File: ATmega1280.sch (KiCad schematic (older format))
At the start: 24 parts, among them CON1 AVR-ISP-10, CON2 AVR-JTAG-10, IC1 ATMEGA1280-A, P1 CONN_02X20, P3 CONN_01X03, P4 CONN_01X03, SW1 SW_PUSH, U1 74HCT541_PWR, U6 WS2812, U7 WS2812, U8 WS2812, X1 CRYSTAL

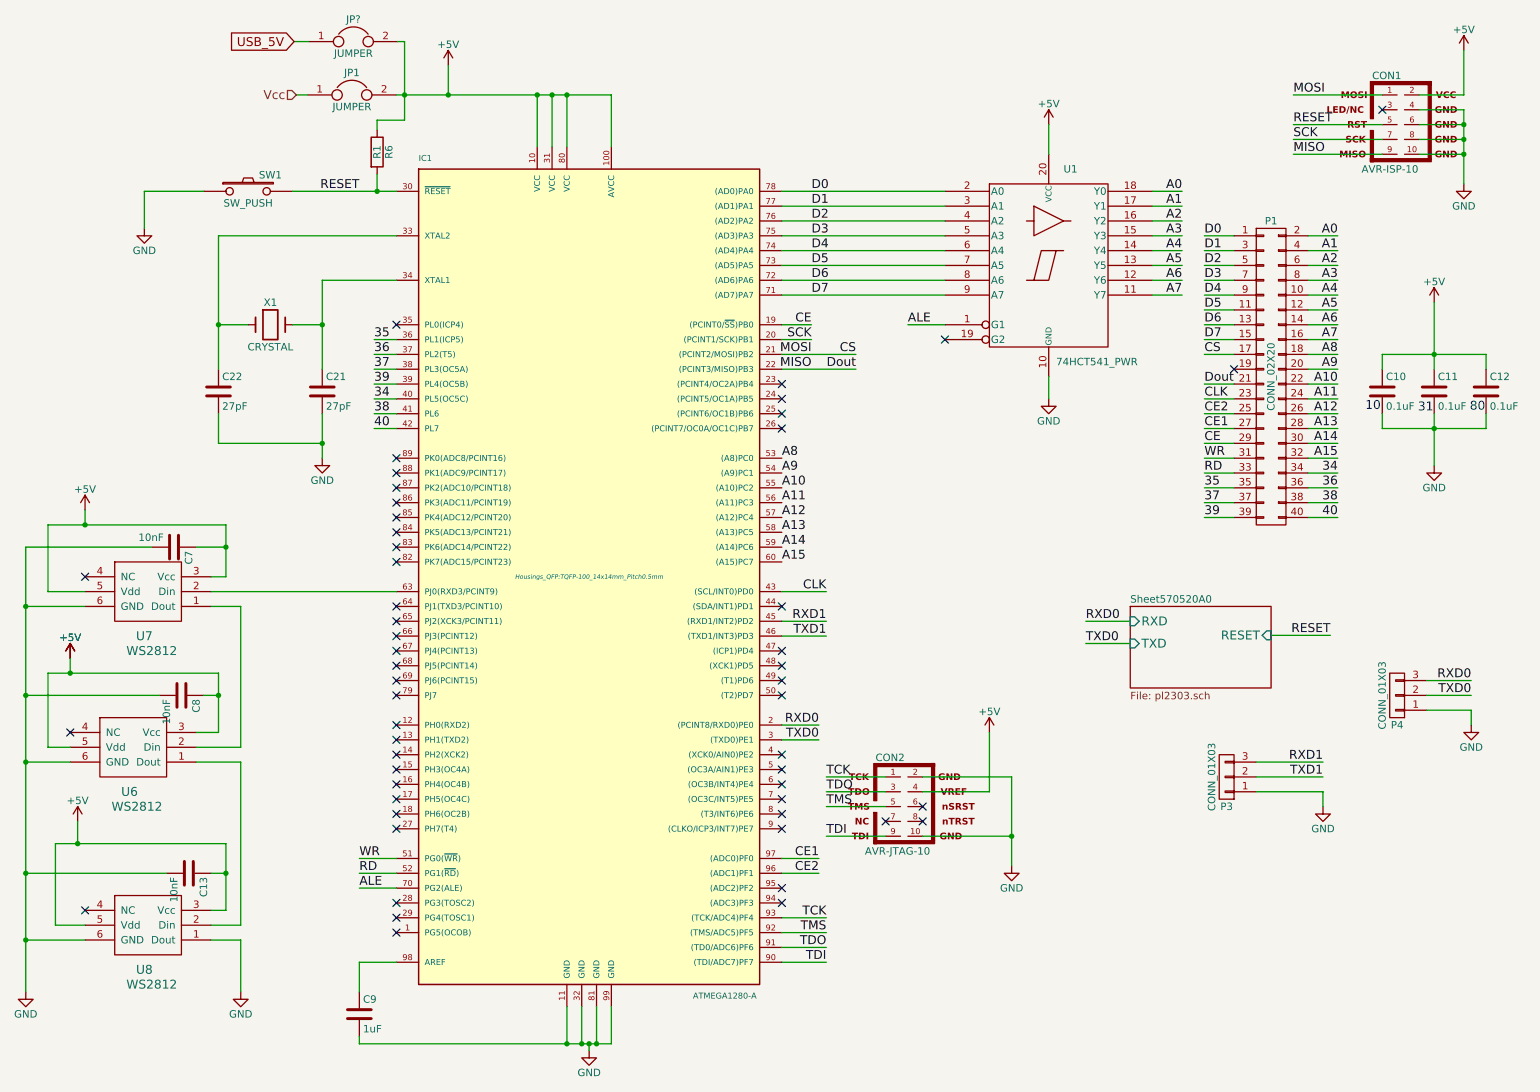
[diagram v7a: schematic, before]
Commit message: Добавлен AMS1117 и изменения в питании
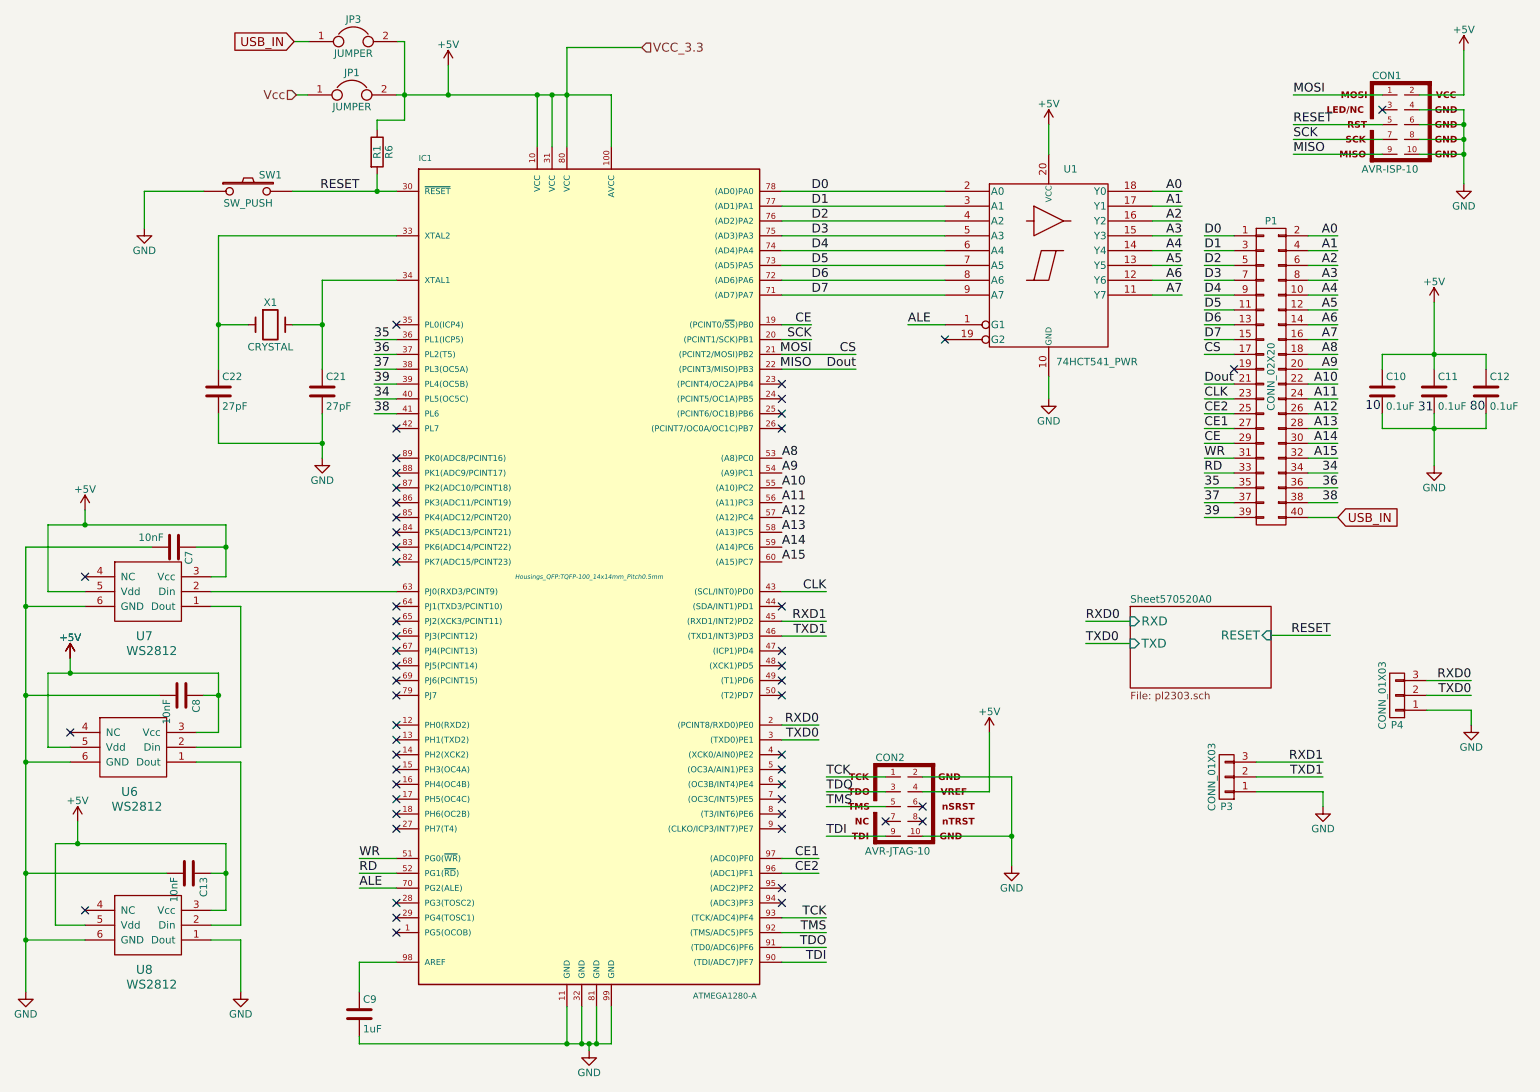
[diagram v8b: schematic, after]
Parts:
- JP3: renamed from JP?; footprint (none) -> Connect:PINHEAD1-2
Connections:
- net 40: no longer names the net of IC1.42 (PL7)
- net 40: no longer P1.40 (P40)
- net USB_5V renamed USB_IN
- net USB_IN: now also P1.40 (P40)
- no-connect marks 53 -> 54
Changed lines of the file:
@@
 $Descr A4 11693 8268
 encoding utf-8
-Sheet 2 4
+Sheet 3 4
 Title ""
 Date "20 apr 2016"
@@
 $EndComp
 $Comp
-L ATMEGA1280-A IC1
-U 1 1 56DEFC46
-P 4450 4350
-F 0 "IC1" H 3300 7150 40  0000 L BNN
-F 1 "ATMEGA1280-A" H 5150 1500 40  0000 L BNN
-F 2 "Housings_QFP:TQFP-100_14x14mm_Pitch0.5mm" H 4450 4350 30  0000 C CIN
-F 3 "" H 4450 4350 60  0000 C CNN
-	1    4450 4350
-	1    0    0    -1
-$EndComp
-$Comp
-L +5V #PWR02
+L +5V #PWR07
 U 1 1 56E703CC
 P 3500 900
-F 0 "#PWR02" H 3500 750 50  0001 C CNN
+F 0 "#PWR07" H 3500 750 50  0001 C CNN
 F 1 "+5V" H 3500 1040 50  0000 C CNN
 F 2 "" H 3500 900 50  0000 C CNN
@@
 $EndComp
 $Comp
-L GND #PWR03
+L GND #PWR08
 U 1 1 56E704E1
 P 4450 7545
-F 0 "#PWR03" H 4450 7295 50  0001 C CNN
+F 0 "#PWR08" H 4450 7295 50  0001 C CNN
 F 1 "GND" H 4450 7395 50  0000 C CNN
 F 2 "" H 4450 7545 50  0000 C CNN
@@
 $EndComp
 $Comp
-L GND #PWR04
+L GND #PWR09
 U 1 1 56E707E0
 P 2650 3550
-F 0 "#PWR04" H 2650 3300 50  0001 C CNN
+F 0 "#PWR09" H 2650 3300 50  0001 C CNN
 F 1 "GND" H 2650 3400 50  0000 C CNN
 F 2 "" H 2650 3550 50  0000 C CNN
@@
 $EndComp
 $Comp
-L GND #PWR05
+L GND #PWR010
 U 1 1 56E70DCE
 P 10150 3600
-F 0 "#PWR05" H 10150 3350 50  0001 C CNN
+F 0 "#PWR010" H 10150 3350 50  0001 C CNN
 F 1 "GND" H 10150 3450 50  0000 C CNN
 F 2 "" H 10150 3600 50  0000 C CNN
@@
 MISO
 $Comp
-L GND #PWR06
+L GND #PWR011
 U 1 1 56E711C0
 P 10350 1700
-F 0 "#PWR06" H 10350 1450 50  0001 C CNN
+F 0 "#PWR011" H 10350 1450 50  0001 C CNN
 F 1 "GND" H 10350 1550 50  0000 C CNN
 F 2 "" H 10350 1700 50  0000 C CNN
@@
 RESET
 $Comp
-L +5V #PWR07
+L +5V #PWR012
 U 1 1 56E711D2
 P 10350 800
-F 0 "#PWR07" H 10350 650 50  0001 C CNN
+F 0 "#PWR012" H 10350 650 50  0001 C CNN
 F 1 "+5V" H 10350 940 50  0000 C CNN
 F 2 "" H 10350 800 50  0000 C CNN
@@
 Vcc
 $Comp
-L +5V #PWR08
+L +5V #PWR013
 U 1 1 56F4EFCF
 P 10150 2500
-F 0 "#PWR08" H 10150 2350 50  0001 C CNN
+F 0 "#PWR013" H 10150 2350 50  0001 C CNN
 F 1 "+5V" H 10150 2640 50  0000 C CNN
 F 2 "" H 10150 2500 50  0000 C CNN
@@
 $EndComp
 $Comp
-L GND #PWR09
+L GND #PWR014
 U 1 1 56F4F102
 P 1450 2000
-F 0 "#PWR09" H 1450 1750 50  0001 C CNN
+F 0 "#PWR014" H 1450 1750 50  0001 C CNN
 F 1 "GND" H 1450 1850 50  0000 C CNN
 F 2 "" H 1450 2000 50  0000 C CNN
@@
 A7
 $Comp
-L GND #PWR010
+L GND #PWR015
 U 1 1 5706A0E3
 P 7550 3150
-F 0 "#PWR010" H 7550 2900 50  0001 C CNN
+F 0 "#PWR015" H 7550 2900 50  0001 C CNN
 F 1 "GND" H 7550 3000 50  0000 C CNN
 F 2 "" H 7550 3150 50  0000 C CNN
@@
 NoConn ~ 3150 4550
 $Comp
-L GND #PWR011
+L GND #PWR016
 U 1 1 5717E47B
 P 9400 5900
-F 0 "#PWR011" H 9400 5650 50  0001 C CNN
+F 0 "#PWR016" H 9400 5650 50  0001 C CNN
 F 1 "GND" H 9400 5750 50  0000 C CNN
 F 2 "" H 9400 5900 50  0000 C CNN
@@
 TXD0
 $Comp
-L GND #PWR012
+L GND #PWR017
 U 1 1 571E463B
 P 10400 5350
-F 0 "#PWR012" H 10400 5100 50  0001 C CNN
+F 0 "#PWR017" H 10400 5100 50  0001 C CNN
 F 1 "GND" H 10400 5200 50  0000 C CNN
 F 2 "" H 10400 5350 50  0000 C CNN
@@
 $EndComp
 $Comp
-L +5V #PWR013
+L +5V #PWR018
 U 1 1 571E941D
 P 1050 3900
-F 0 "#PWR013" H 1050 3750 50  0001 C CNN
+F 0 "#PWR018" H 1050 3750 50  0001 C CNN
 F 1 "+5V" H 1050 4040 50  0000 C CNN
 F 2 "" H 1050 3900 50  0000 C CNN
@@
 $EndComp
 $Comp
-L GND #PWR014
+L GND #PWR019
 U 1 1 571E963E
 P 650 7150
-F 0 "#PWR014" H 650 6900 50  0001 C CNN
+F 0 "#PWR019" H 650 6900 50  0001 C CNN
 F 1 "GND" H 650 7000 50  0000 C CNN
 F 2 "" H 650 7150 50  0000 C CNN
@@
 $EndComp
 $Comp
-L +5V #PWR015
+L +5V #PWR020
 U 1 1 571EC74C
 P 950 4900
-F 0 "#PWR015" H 950 4750 50  0001 C CNN
+F 0 "#PWR020" H 950 4750 50  0001 C CNN
 F 1 "+5V" H 950 5040 50  0000 C CNN
 F 2 "" H 950 4900 50  0000 C CNN
@@
 $EndComp
 $Comp
-L +5V #PWR016
+L +5V #PWR021
 U 1 1 571EC7A2
 P 950 4900
-F 0 "#PWR016" H 950 4750 50  0001 C CNN
+F 0 "#PWR021" H 950 4750 50  0001 C CNN
 F 1 "+5V" H 950 5040 50  0000 C CNN
 F 2 "" H 950 4900 50  0000 C CNN
@@
 $EndComp
 $Comp
-L +5V #PWR017
+L +5V #PWR022
 U 1 1 571EC7E1
 P 1000 6000
-F 0 "#PWR017" H 1000 5850 50  0001 C CNN
+F 0 "#PWR022" H 1000 5850 50  0001 C CNN
 F 1 "+5V" H 1000 6140 50  0000 C CNN
 F 2 "" H 1000 6000 50  0000 C CNN
@@
 NoConn ~ 1050 6600
 $Comp
-L GND #PWR018
+L GND #PWR023
 U 1 1 571EDCF8
 P 2100 7150
-F 0 "#PWR018" H 2100 6900 50  0001 C CNN
+F 0 "#PWR023" H 2100 6900 50  0001 C CNN
 F 1 "GND" H 2100 7000 50  0000 C CNN
 F 2 "" H 2100 7150 50  0000 C CNN
@@
 $EndComp
 $Comp
-L +5V #PWR019
+L +5V #PWR024
 U 1 1 571EE571
 P 7550 1300
-F 0 "#PWR019" H 7550 1150 50  0001 C CNN
+F 0 "#PWR024" H 7550 1150 50  0001 C CNN
 F 1 "+5V" H 7550 1440 50  0000 C CNN
 F 2 "" H 7550 1300 50  0000 C CNN
@@
 NoConn ~ 6450 6000
 $Comp
-L GND #PWR020
+L GND #PWR025
 U 1 1 57212B56
 P 7300 6300
-F 0 "#PWR020" H 7300 6050 50  0001 C CNN
+F 0 "#PWR025" H 7300 6050 50  0001 C CNN
 F 1 "GND" H 7300 6150 50  0000 C CNN
 F 2 "" H 7300 6300 50  0000 C CNN
@@
 $EndComp
 $Comp
-L +5V #PWR021
+L +5V #PWR026
 U 1 1 57212CB0
 P 7150 5400
-F 0 "#PWR021" H 7150 5250 50  0001 C CNN
+F 0 "#PWR026" H 7150 5250 50  0001 C CNN
 F 1 "+5V" H 7150 5540 50  0000 C CNN
 F 2 "" H 7150 5400 50  0000 C CNN
@@
 Text Label 9500 3850 2    60   ~ 0
 38
-Text Label 9500 3950 2    60   ~ 0
-40
 Text Label 3000 3250 0    60   ~ 0
 38
-Text Label 3000 3350 0    60   ~ 0
-40
 NoConn ~ 3150 3550
 NoConn ~ 3150 3650
@@
 Connection ~ 4100 1100
 Wire Wire Line
-	4300 1100 4300 1450
+	4300 780  4300 1450
 Connection ~ 4200 1100
 Connection ~ 4300 1100
@@
 	3150 3250 3000 3250
 Wire Wire Line
-	3150 3350 3000 3350
-Wire Wire Line
 	5750 6250 6000 6250
 Wire Wire Line
@@
 	3020 1335 3020 1270
 Wire Wire Line
-	3205 1270 3020 1270
-Wire Wire Line
-	3205 740  3205 1270
+	3020 1270 3205 1270
+Wire Wire Line
+	3205 1270 3205 740
 Connection ~ 3205 1100
 Text GLabel 2460 740  0    60   Input ~ 0
-USB_5V
-$Comp
-L JUMPER JP?
+USB_IN
+$Comp
+L JUMPER JP3
 U 1 1 578E6590
 P 2860 740
-F 0 "JP?" H 2860 890 50  0000 C CNN
+F 0 "JP3" H 2860 890 50  0000 C CNN
 F 1 "JUMPER" H 2860 660 50  0000 C CNN
-F 2 "" H 2860 740 50  0000 C CNN
+F 2 "Connect:PINHEAD1-2" H 2860 740 50  0001 C CNN
 F 3 "" H 2860 740 50  0000 C CNN
 	1    2860 740
@@
 	2460 740  2560 740
 Wire Wire Line
-	3160 740  3205 740
+	3205 740  3160 740
+$Comp
+L ATMEGA1280-A IC1
+U 1 1 56DEFC46
+P 4450 4350
+F 0 "IC1" H 3300 7150 40  0000 L BNN
+F 1 "ATMEGA1280-A" H 5150 1500 40  0000 L BNN
+F 2 "Housings_QFP:TQFP-100_14x14mm_Pitch0.5mm" H 4450 4350 30  0000 C CIN
+F 3 "" H 4450 4350 60  0000 C CNN
+	1    4450 4350
+	1    0    0    -1
+$EndComp
+NoConn ~ 3150 3350
+Text GLabel 9500 3950 2    60   Input ~ 0
+USB_IN
+Text HLabel 4805 780  2    60   Input ~ 0
+VCC_3.3
+Wire Wire Line
+	4805 780  4300 780
 $EndSCHEMATC
